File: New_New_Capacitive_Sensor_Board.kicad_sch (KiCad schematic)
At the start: 11 parts, among them J1 Conn_01x04_Pin, J3 Conn_01x06_Pin, U1 FDC2212QDNTTQ1

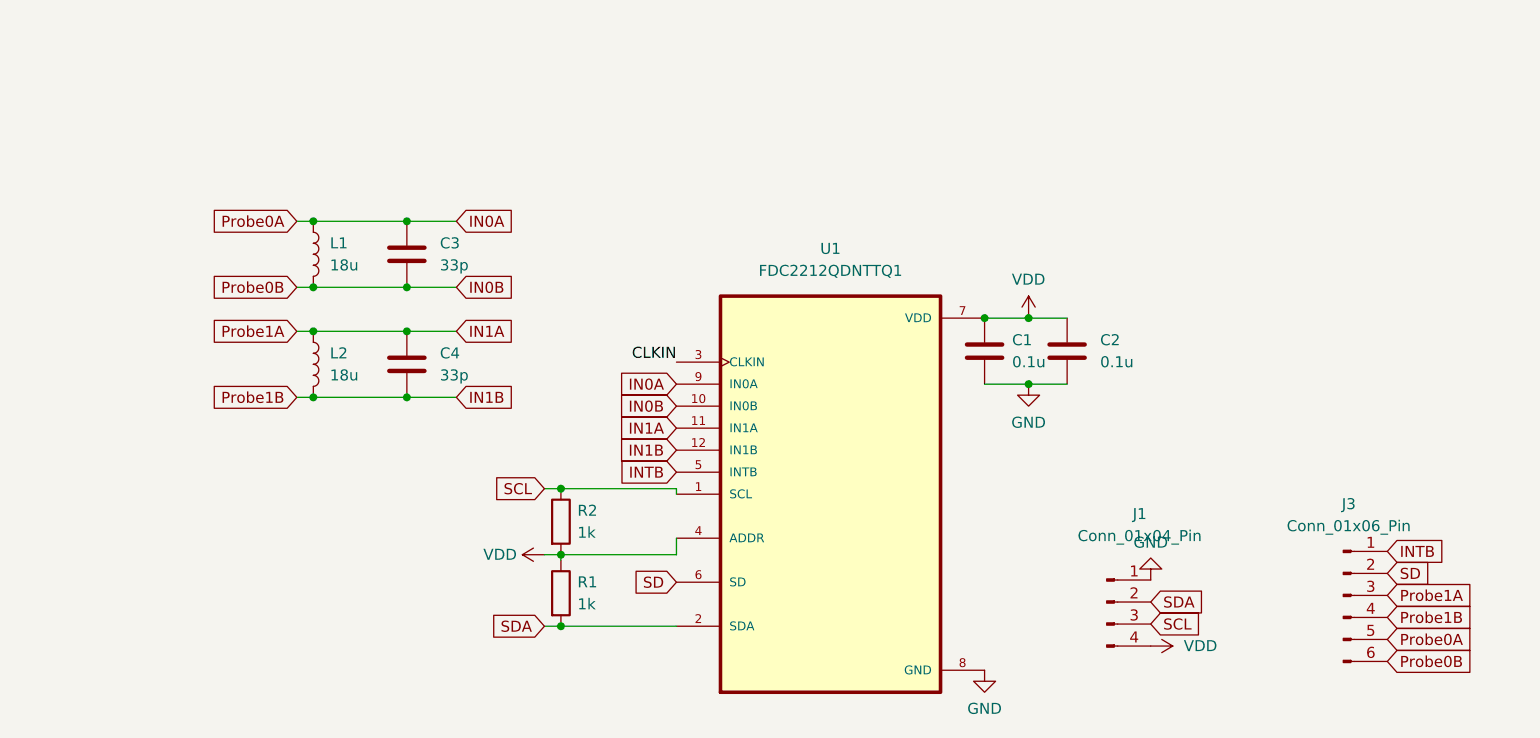
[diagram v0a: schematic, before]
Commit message: Schematic changes specified in design review
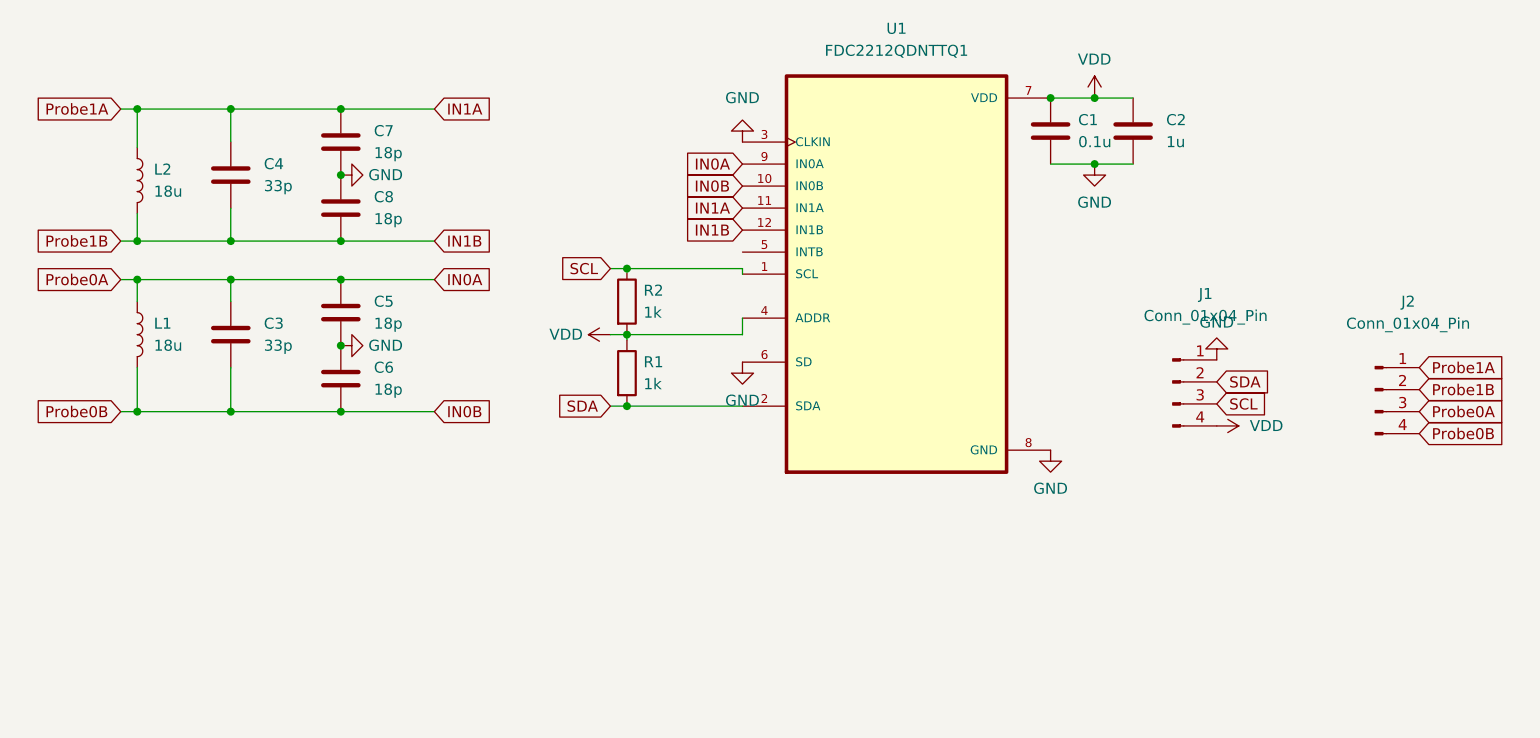
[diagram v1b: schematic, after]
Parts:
- removed J3: Conn_01x06_Pin, Connector_JST:JST_XH_S6B-XH-A_1x06_P2.50mm_Horizontal, symbol Connector:Conn_01x06_Pin
- added C5, C6, C7, C8: 18p, Capacitor_SMD:C_0402_1005Metric, symbol Device:C
- added J2: Conn_01x04_Pin, Connector_JST:JST_XH_S4B-XH-A_1x04_P2.50mm_Horizontal, symbol Connector:Conn_01x04_Pin
- C2: value 0.1u -> 1u
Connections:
- net CLKIN is gone; now on net GND: U1.3 (CLKIN)
- net SD is gone; now on net GND: U1.6 (SD)
- net GND: now also C5.2, C6.1, C7.2, C8.1
- net IN0A: now also C5.1, J2.3 (Pin_3)
- net IN0B: now also C6.2, J2.4 (Pin_4)
- net IN1A: now also C7.1, J2.1 (Pin_1)
- net IN1B: now also C8.2, J2.2 (Pin_2)
- net INTB: no longer names the net of U1.5 (INTB)
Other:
- moved on the sheet: C1, C2, C3, C4, J1, L1, L2, R1, R2, U1

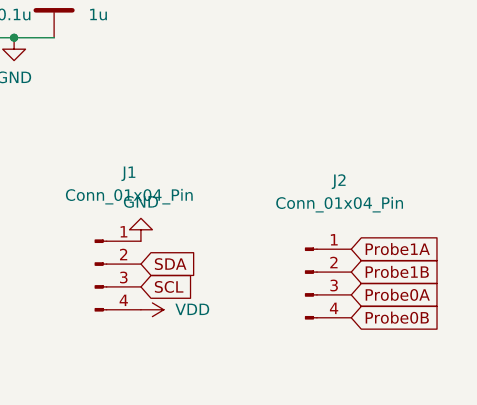
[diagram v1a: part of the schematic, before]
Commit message: Update PCB Design as per Design Review
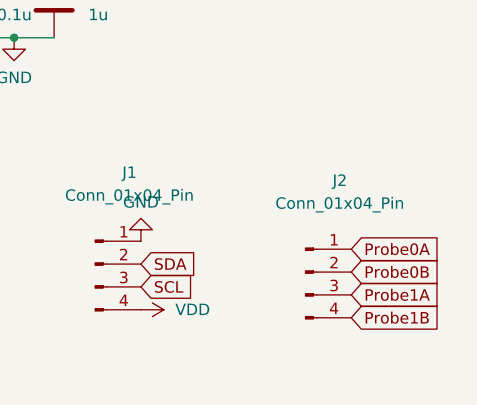
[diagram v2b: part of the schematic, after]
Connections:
- net IN0A: now also J2.1 (Pin_1); no longer J2.3 (Pin_3)
- net IN0B: now also J2.2 (Pin_2); no longer J2.4 (Pin_4)
- net IN1A: now also J2.3 (Pin_3); no longer J2.1 (Pin_1)
- net IN1B: now also J2.4 (Pin_4); no longer J2.2 (Pin_2)
